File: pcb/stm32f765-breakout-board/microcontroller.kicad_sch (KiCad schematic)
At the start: 9 parts, among them SW2 SW_BOOT0, U1 STM32F765VIT6, Y1 16MHz

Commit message: added lsm6dsl to pcb and ordered v3
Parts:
- added C18, C19: 100n, Capacitor_SMD:C_0805_2012Metric_Pad1.18x1.45mm_HandSolder, symbol Device:C_Small
- added U4: LSM6DSL, Package_LGA:LGA-14_3x2.5mm_P0.5mm_LayoutBorder3x4y, symbol Sensor_Motion:LSM6DSL
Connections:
- net +3.3VA: now also U1.20 (VREF+)
- net +3V3: now also C18.1, C19.1, U4.12 (CS), U4.5 (VDDIO), U4.8 (VDD)
- net GND: now also C18.2, C19.2, U4.1 (SDO/SA0), U4.2 (SDX), U4.3 (SCX), U4.6 (GND), U4.7 (GND)
- net I2C2_SCL: now also U4.13 (SCL)
- net I2C2_SDA: now also U4.14 (SDA)
- no-connect marks 38 -> 39
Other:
- note added: "LSM6DSL 6-Axis IMU"
- moved on the sheet: R2, SW2

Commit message: final breakout board ordered
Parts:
- added H1: MountingHole_Pad, MountingHole:MountingHole_2.2mm_M2_Pad, symbol Mechanical:MountingHole_Pad
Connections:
- net GND: now also H1.1
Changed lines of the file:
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@@
 	(wire
 		(pts
+			(xy 44.45 157.48) (xy 44.45 161.29)
+		)
+		(stroke
+			(width 0)
+			(type default)
+		)
+	)
+	(wire
+		(pts
 			(xy 59.69 66.04) (xy 52.07 66.04)
 		)
@@
 	)
 	(symbol
+		(lib_id "Mechanical:MountingHole_Pad")
+		(at 44.45 154.94 0)
+		(unit 1)
+		(exclude_from_sim no)
+		(in_bom no)
+		(on_board yes)
+		(dnp no)
+		(fields_autoplaced yes)
+		(property "Reference" "H1"
+			(at 46.99 152.3999 0)
+			(effects
+				(font
+					(size 1.27 1.27)
+				)
+				(justify left)
+			)
+		)
+		(property "Value" "MountingHole_Pad"
+			(at 46.99 154.9399 0)
+			(effects
+				(font
+					(size 1.27 1.27)
+				)
+				(justify left)
+			)
+		)
+		(property "Footprint" "MountingHole:MountingHole_2.2mm_M2_Pad"
+			(at 44.45 154.94 0)
+			(effects
+				(font
+					(size 1.27 1.27)
+				)
+				(hide yes)
+			)
+		)
+		(property "Datasheet" "~"
+			(at 44.45 154.94 0)
+			(effects
+				(font
+					(size 1.27 1.27)
+				)
+				(hide yes)
+			)
+		)
+		(property "Description" "Mounting Hole with connection"
+			(at 44.45 154.94 0)
+			(effects
+				(font
+					(size 1.27 1.27)
+				)
+				(hide yes)
+			)
+		)
+		(pin "1"
+		)
+		(instances
+			(project "stm32f765-breakout-board"
+				(path "/256bcd66-93a7-4ec7-b605-dbc945027d42/700d8081-3af4-47b1-ac9b-f87f9ce01503"
+					(reference "H1")
+					(unit 1)
+				)
+			)
+		)
+	)
+	(symbol
 		(lib_id "Sensor_Motion:LSM6DSL")
 		(at 241.3 118.11 0)
@@
 					(unit 1)
 				)
+			)
+		)
+	)
+	(symbol
+		(lib_id "power:GND")
+		(at 44.45 161.29 0)
+		(unit 1)
+		(exclude_from_sim no)
+		(in_bom yes)
+		(on_board yes)
+		(dnp no)
+		(fields_autoplaced yes)
+		(property "Reference" "#PWR031"
+			(at 44.45 167.64 0)
+			(effects
+				(font
+					(size 1.27 1.27)
+				)
+				(hide yes)
+			)
+		)
+		(property "Value" "GND"
+			(at 44.45 166.37 0)
+			(effects
+				(font
+					(size 1.27 1.27)
+				)
+			)
+		)
+		(property "Footprint" ""
+			(at 44.45 161.29 0)
+			(effects
+				(font
+					(size 1.27 1.27)
+				)
+				(hide yes)
+			)
+		)
+		(property "Datasheet" ""
+			(at 44.45 161.29 0)
+			(effects
+				(font
+					(size 1.27 1.27)
+				)
+				(hide yes)
+			)
+		)
+		(property "Description" "Power symbol creates a global label with name \"GND\" , ground"
+			(at 44.45 161.29 0)
+			(effects
+				(font
+					(size 1.27 1.27)
+				)
+				(hide yes)
+			)
+		)
+		(pin "1"
+		)
+		(instances
+			(project "stm32f765-breakout-board"
+				(path "/256bcd66-93a7-4ec7-b605-dbc945027d42/700d8081-3af4-47b1-ac9b-f87f9ce01503"
+					(reference "#PWR031")
+					(unit 1)
+				)

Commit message: Updated titleblock on f765 breakout pcb
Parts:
- H1: value MountingHole_Pad -> GND
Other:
- note added: "Ground Pad for Testing"
- company: (none) -> Pranav Chandra N. V.
- title: (none) -> STM32F765VIT6 Breakout Board
- moved on the sheet: H1
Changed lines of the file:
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@@
 	(generator_version "9.0")
 	(paper "A4")
+	(title_block
+		(title "STM32F765VIT6 Breakout Board")
+		(date "2026-04-17")
+		(rev "v5")
+		(company "Pranav Chandra N. V.")
+		(comment 1 "v4: Added Grounding Pad")
+	)
 	(text "Crystal Capacitance = 9pF\nAssumed Stray Capacitance = 4pF\n\nStabilizing Capacitance = (9pf - 4pF) * 2 = 10pF"
 		(exclude_from_sim no)
@@
 		)
 	)
+	(text "Ground Pad for Testing"
+		(exclude_from_sim no)
+		(at 44.958 163.83 0)
+		(effects
+			(font
+				(size 1.27 1.27)
+			)
+		)
+	)
 	(junction
 		(at 116.84 27.94)
@@
 	(wire
 		(pts
-			(xy 44.45 157.48) (xy 44.45 161.29)
+			(xy 43.18 147.32) (xy 43.18 151.13)
 		)
 		(stroke
@@
 		(polyline
 			(pts
+				(xy 24.13 131.445) (xy 64.77 131.445) (xy 64.77 165.735) (xy 24.13 165.735)
+			)
+			(stroke
+				(width 0)
+				(type dash)
+			)
+			(fill
+				(type none)
+			)
+		)
+	)
+	(rule_area
+		(polyline
+			(pts
 				(xy 205.105 37.6238) (xy 254.635 37.3062) (xy 254.635 70.1674) (xy 205.105 70.485)
 			)
@@
 	(symbol
 		(lib_id "Mechanical:MountingHole_Pad")
-		(at 44.45 154.94 0)
+		(at 43.18 144.78 0)
 		(unit 1)
 		(exclude_from_sim no)
@@
 		(on_board yes)
 		(dnp no)
-		(fields_autoplaced yes)
 		(property "Reference" "H1"
-			(at 46.99 152.3999 0)
+			(at 44.45 140.716 0)
 			(effects
 				(font
@@
 			)
 		)
-		(property "Value" "MountingHole_Pad"
-			(at 46.99 154.9399 0)
+		(property "Value" "GND"
+			(at 43.688 146.558 0)
 			(effects
 				(font
@@
 		)
 		(property "Footprint" "MountingHole:MountingHole_2.2mm_M2_Pad"
-			(at 44.45 154.94 0)
+			(at 43.18 144.78 0)
 			(effects
 				(font
@@
 		)
 		(property "Datasheet" "~"
-			(at 44.45 154.94 0)
+			(at 43.18 144.78 0)
 			(effects
 				(font
@@
 		)
 		(property "Description" "Mounting Hole with connection"
-			(at 44.45 154.94 0)
+			(at 43.18 144.78 0)
 			(effects
 				(font
@@
 	(symbol
 		(lib_id "power:GND")
-		(at 44.45 161.29 0)
+		(at 43.18 151.13 0)
 		(unit 1)
 		(exclude_from_sim no)
@@
 		(fields_autoplaced yes)
 		(property "Reference" "#PWR031"
-			(at 44.45 167.64 0)
+			(at 43.18 157.48 0)
 			(effects
 				(font
@@
 		)
 		(property "Value" "GND"
-			(at 44.45 166.37 0)
+			(at 43.18 156.21 0)
 			(effects
 				(font
@@
 		)
 		(property "Footprint" ""
-			(at 44.45 161.29 0)
+			(at 43.18 151.13 0)
 			(effects
 				(font
@@
 		)
 		(property "Datasheet" ""
-			(at 44.45 161.29 0)
+			(at 43.18 151.13 0)
 			(effects
 				(font
@@
 		)
 		(property "Description" "Power symbol creates a global label with name \"GND\" , ground"
-			(at 44.45 161.29 0)
+			(at 43.18 151.13 0)
 			(effects
 				(font

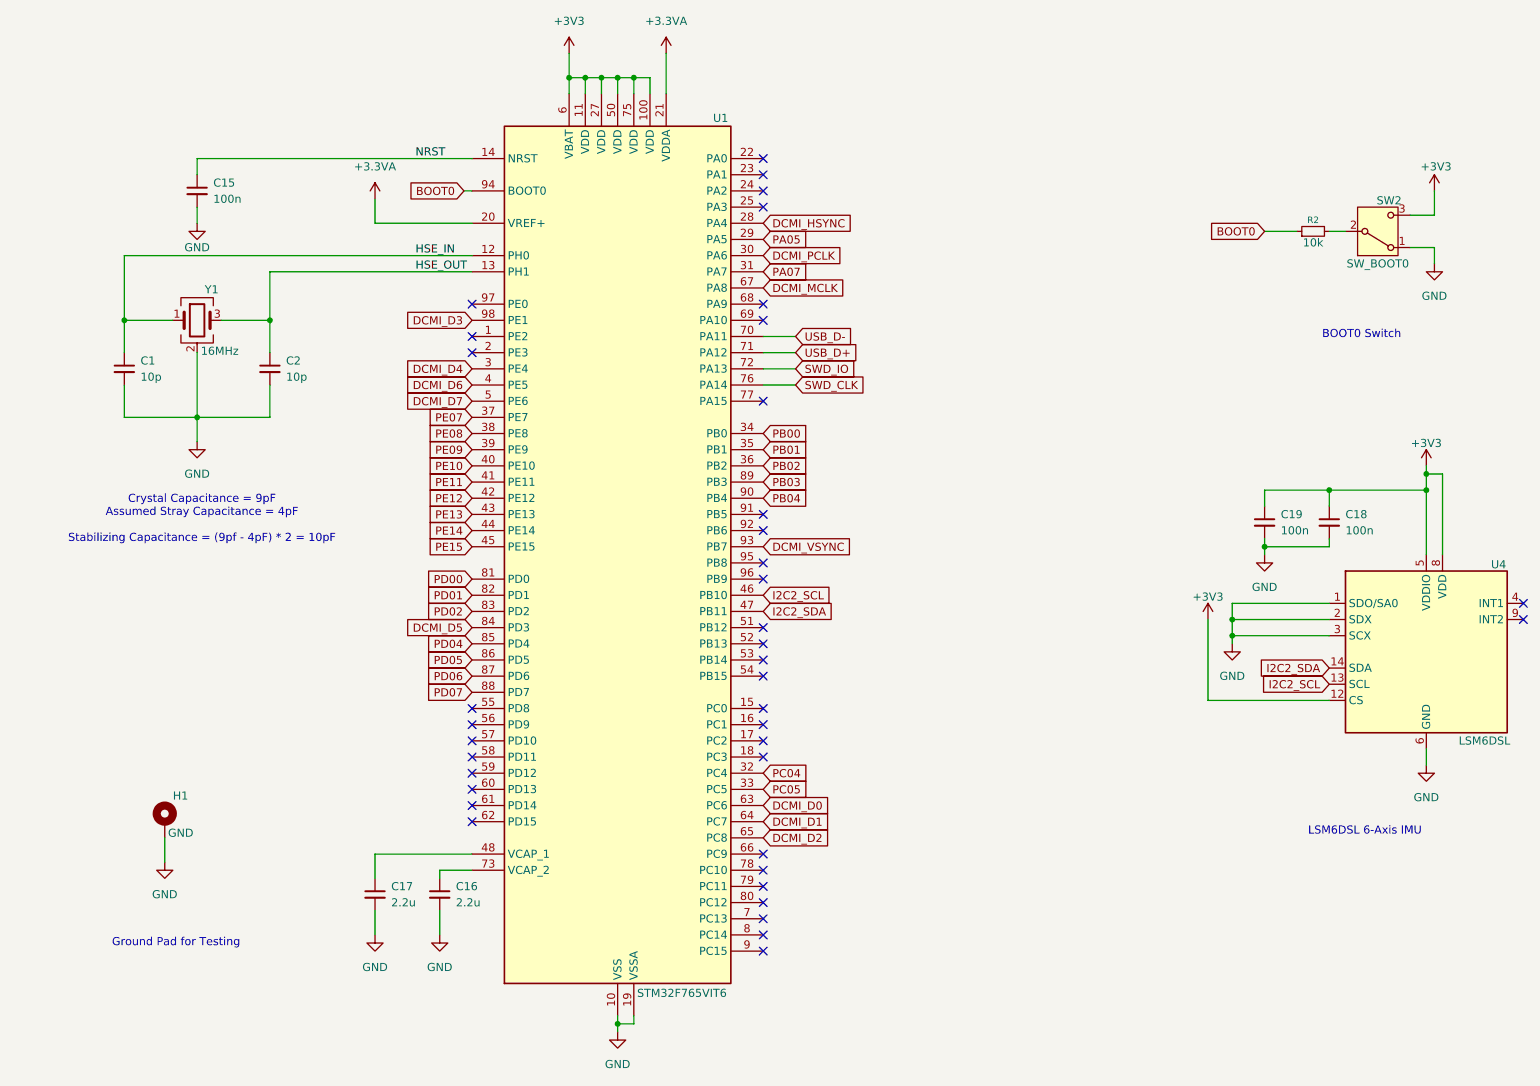
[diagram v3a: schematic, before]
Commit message: Added on board LED to PCB and blinky for board
v6 of the PCB now has an in built on board LED to PE02, to allow for
faster debugging.

The first assembled prototype finally worked, and a blinky sketch was
flashed to test. Relevant code has been added to firmware.
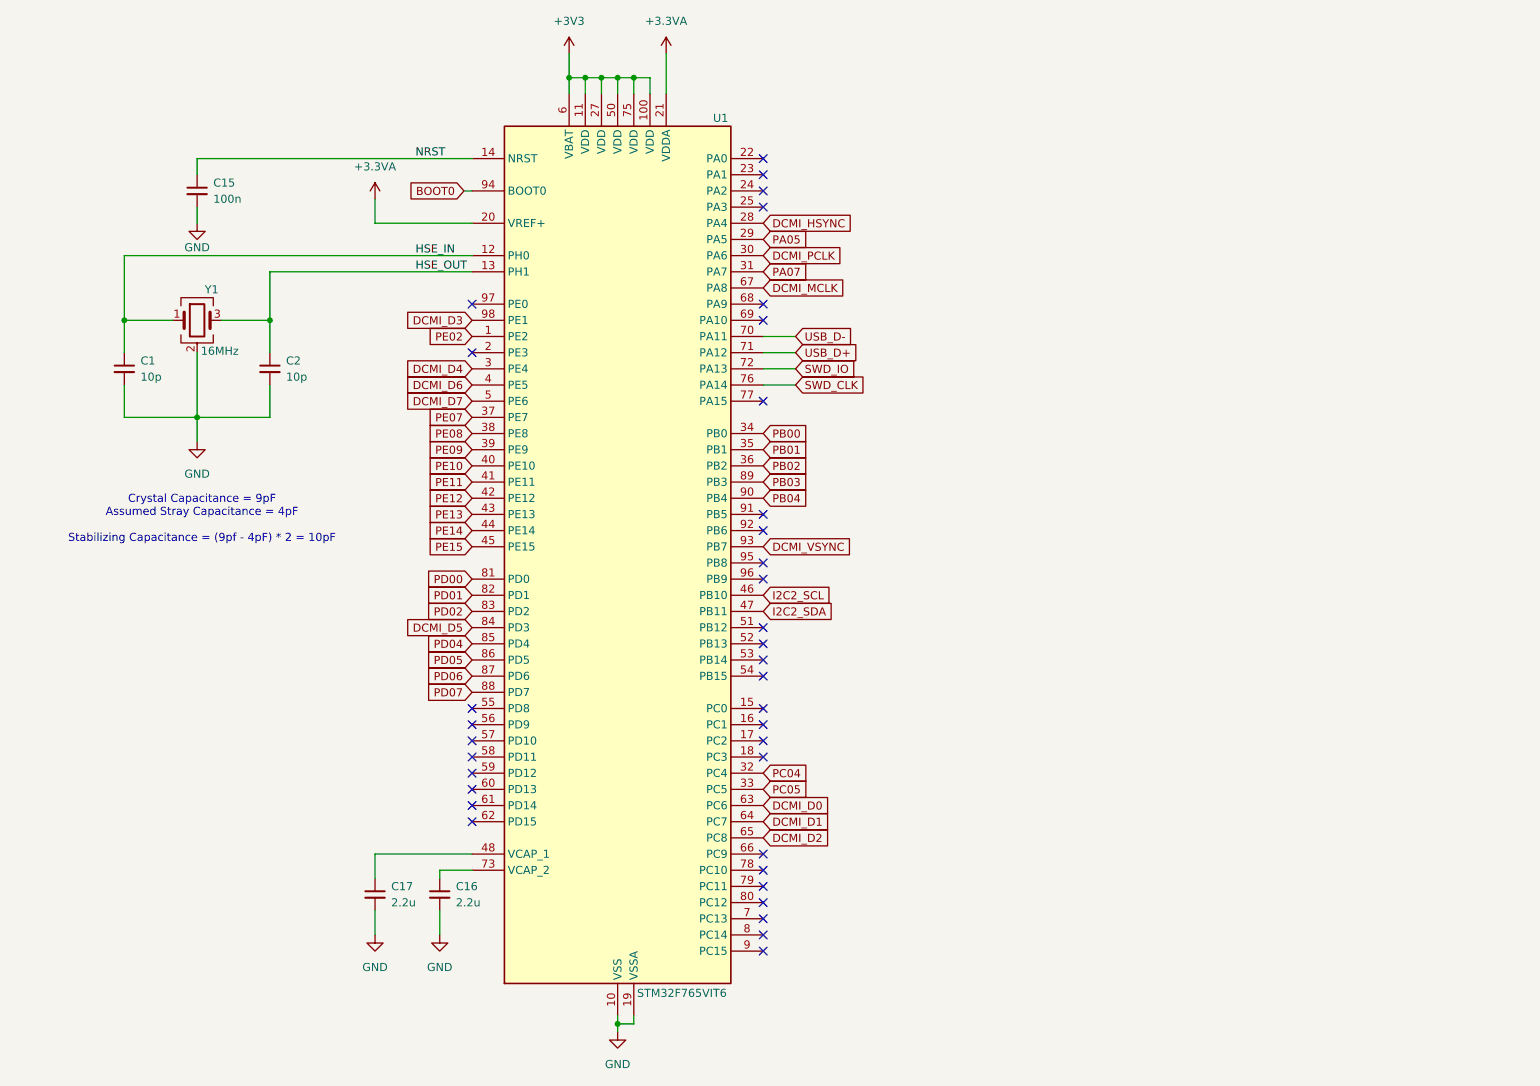
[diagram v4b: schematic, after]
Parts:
- removed C18, C19: 100n, Capacitor_SMD:C_0805_2012Metric_Pad1.18x1.45mm_HandSolder, symbol Device:C_Small
- removed H1: GND, MountingHole:MountingHole_2.2mm_M2_Pad, symbol Mechanical:MountingHole_Pad
- removed R2: 10k, Resistor_SMD:R_0805_2012Metric_Pad1.20x1.40mm_HandSolder, symbol Device:R_Small
- removed SW2: SW_BOOT0, stm32_f765_breakout_library:new_4.5x4.5_mm_tactile_button_1883759, symbol Switch:SW_SPDT
- removed U4: LSM6DSL, Package_LGA:LGA-14_3x2.5mm_P0.5mm_LayoutBorder3x4y, symbol Sensor_Motion:LSM6DSL
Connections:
- net PE02: now reaches U1.1 (PE2)
- no-connect marks 39 -> 36
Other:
- note removed: "BOOT0 Switch"
- note removed: "Ground Pad for Testing"
- note removed: "LSM6DSL 6-Axis IMU"
